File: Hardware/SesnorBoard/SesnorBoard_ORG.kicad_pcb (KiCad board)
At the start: 2 copper layers, 25 parts, among them J1 Mainboard connection, J2 microphoon connection, U1 AMG8833, U2 CCS811, U3 NC7SVU04P5X

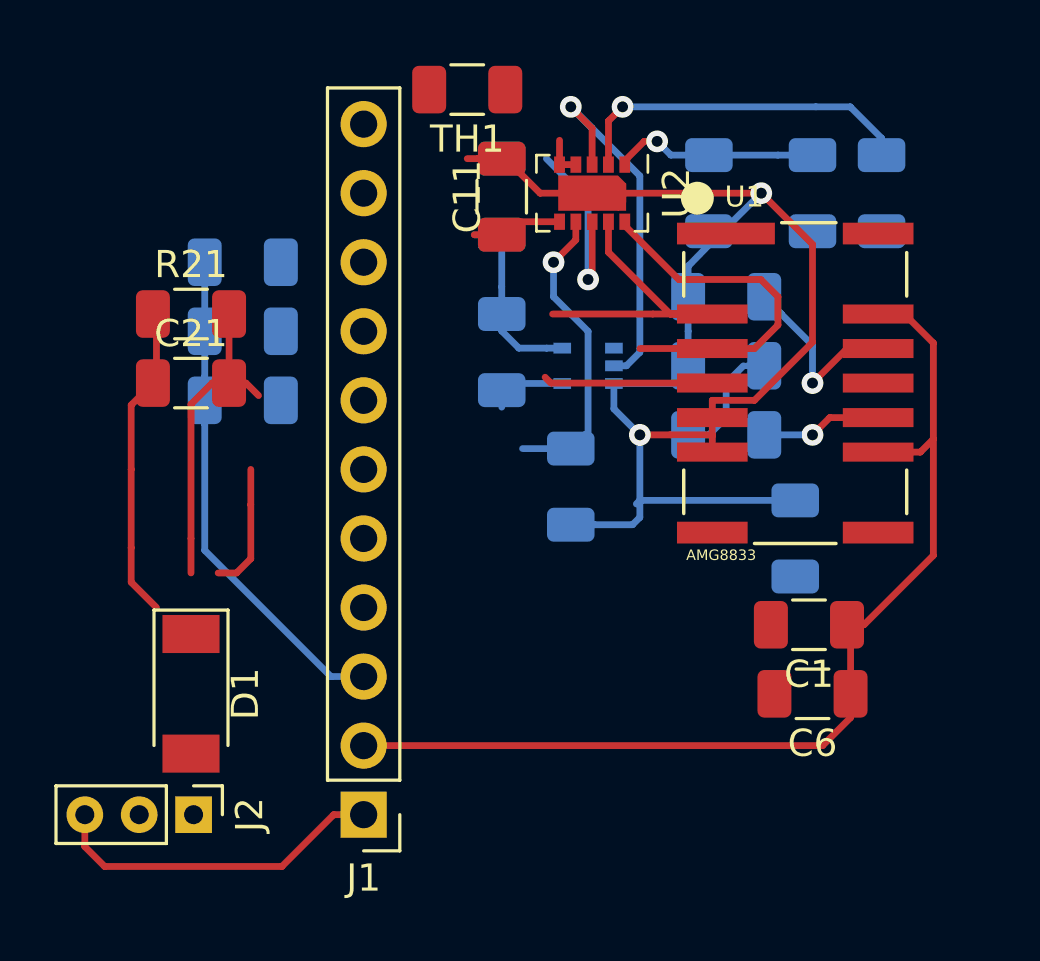
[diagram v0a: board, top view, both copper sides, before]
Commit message: SEnsorboard PCB adapted to normal siezd pinheader
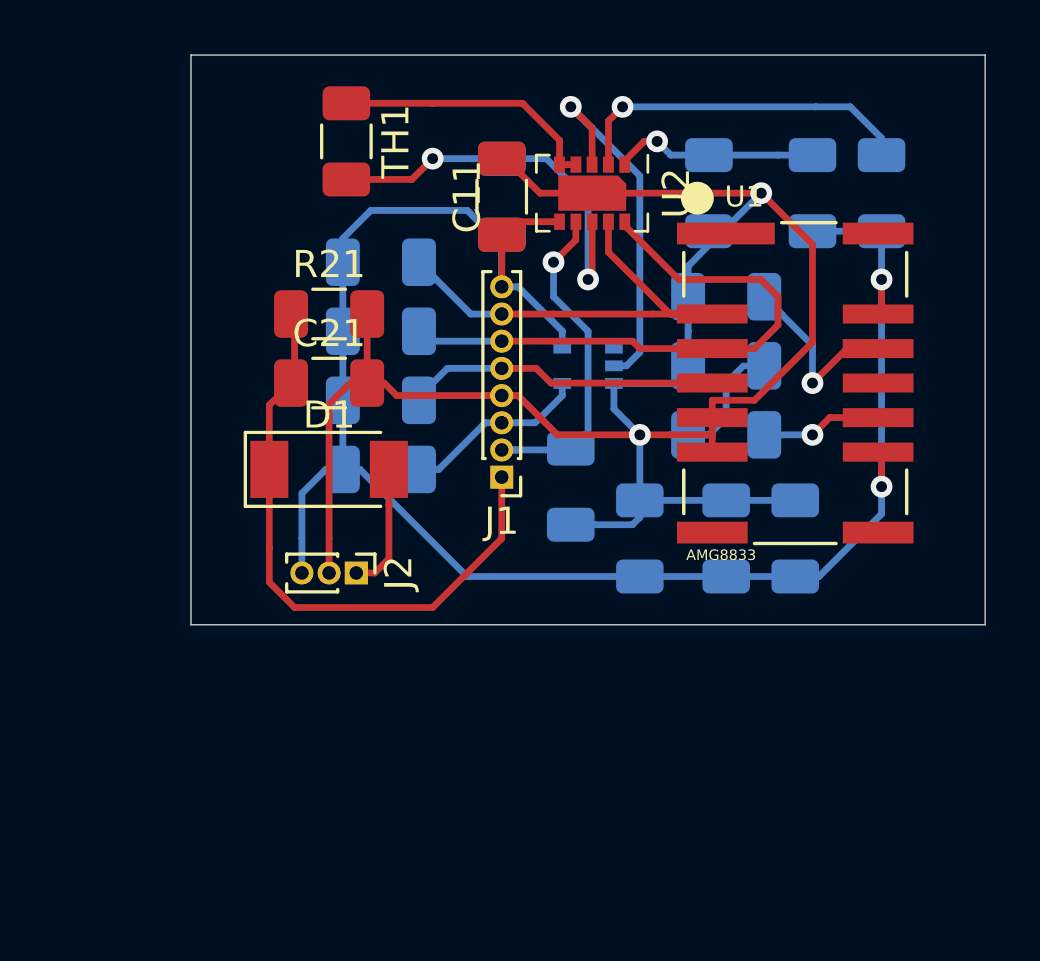
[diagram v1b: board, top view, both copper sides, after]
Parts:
- C1, C6: moved to B.Cu
- J1: footprint Connector_PinHeader_2.54mm:PinHeader_1x11_P2.54mm_Vertical -> Connector_PinHeader_1.00mm:PinHeader_1x08_P1.00mm_Vertical
- J2: footprint Connector_PinHeader_2.00mm:PinHeader_1x03_P2.00mm_Vertical -> Connector_PinHeader_1.00mm:PinHeader_1x03_P1.00mm_Vertical
- moved J1 13.4 mm to (68.6, -307.1)
- moved J2 10.7 mm to (63.2, -303.5)
- moved D1 9.69 mm to (62.2, -307.3), turned to 0 degrees
- moved C6 8.54 mm to (73.7, -304.8), turned to 90 degrees
- moved R16 6.19 mm to (64.1, -307.3), turned to 180 degrees
- moved R1 5.08 mm to (64.1, -309.9)
- moved R3 5.08 mm to (64.1, -315.0)
- moved R4 5.08 mm to (64.1, -312.4)
- moved C21 5.08 mm to (62.2, -310.5)
- moved R21 5.08 mm to (62.2, -313.1)
- moved TH1 4.84 mm to (62.9, -319.4), turned to 270 degrees
- moved C1 4.40 mm to (76.8, -304.8), turned to 90 degrees
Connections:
- C1 pad 1: /AMG8833_3V3 -> 3.3V
- C11 pad 1: /CCS811_3V3 -> 3.3V
- C6 pad 1: /AMG8833_3V3 -> 3.3V
- J1 pad 1: /AUDIO_3V3 -> /DETECTOR_OUT
- J1 pad 2: /AMG8833_3V3 -> /nWAKE
- J1 pad 3: 3.3V -> /nINT_CCS811
- J1 pad 4: /DETECTOR_OUT -> GND
- J1 pad 5: /nWAKE -> /INT_AMG8833
- J1 pad 6: /nINT_CCS811 -> /SCL
- J1 pad 7: GND -> /SDA
- J1 pad 8: /INT_AMG8833 -> 3.3V
- J2 pad 3: /AUDIO_3V3 -> 3.3V
- R12 pad 2: /CCS811_3V3 -> 3.3V
- R13 pad 2: /CCS811_3V3 -> 3.3V
- R16 pad 2: /CCS811_3V3 -> 3.3V
- U1 pad 13: /AMG8833_3V3 -> 3.3V
- U1 pad 9: /AMG8833_3V3 -> 3.3V
- U2 pad 6: /CCS811_3V3 -> 3.3V
- U3 pad 5: /CCS811_3V3 -> 3.3V
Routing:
- net 3.3V: track 18.9 -> 67.2 mm, vias 0 -> 2
- net /AMG8833_3V3: track 39.0 -> 0.00 mm
- net /AUDIO_3V3: track 12.5 -> 0.00 mm
- net /DETECTOR_OUT: track 11.5 -> 22.4 mm
- net /CCS811_3V3: track 10.0 -> 0.00 mm
- net GND: track 63.3 -> 72.2 mm
- net Net-(TH1-Pad1): track 1.49 -> 9.90 mm
- net /SCL: track 13.3 -> 21.7 mm
- net Net-(R12-Pad1): track 7.27 -> 14.9 mm, vias 1 -> 2
- net /SDA: track 11.8 -> 18.0 mm
- net /INT_AMG8833: track 6.37 -> 11.8 mm
- net /nINT_CCS811: track 2.95 -> 6.84 mm
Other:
- board outline added: 29.2 x 21 mm
- board text removed: "All holes are plated holes with finished hole sizes"
